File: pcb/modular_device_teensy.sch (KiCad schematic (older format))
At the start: 17 parts, among them P1 PWR_JACK_2.5x5.5_SMD_RA, P2 HEADER_01X03_SMD_RA, P3 HEADER_01X03_SMD_RA, P4 HEADER_01X03_SMD_RA, P5 BNC_DOUBLE_RA, P6 HEADER_01X02_SMD_RA, P7 HEADER_01X02_SMD_RA, SW1 KT_SWITCH

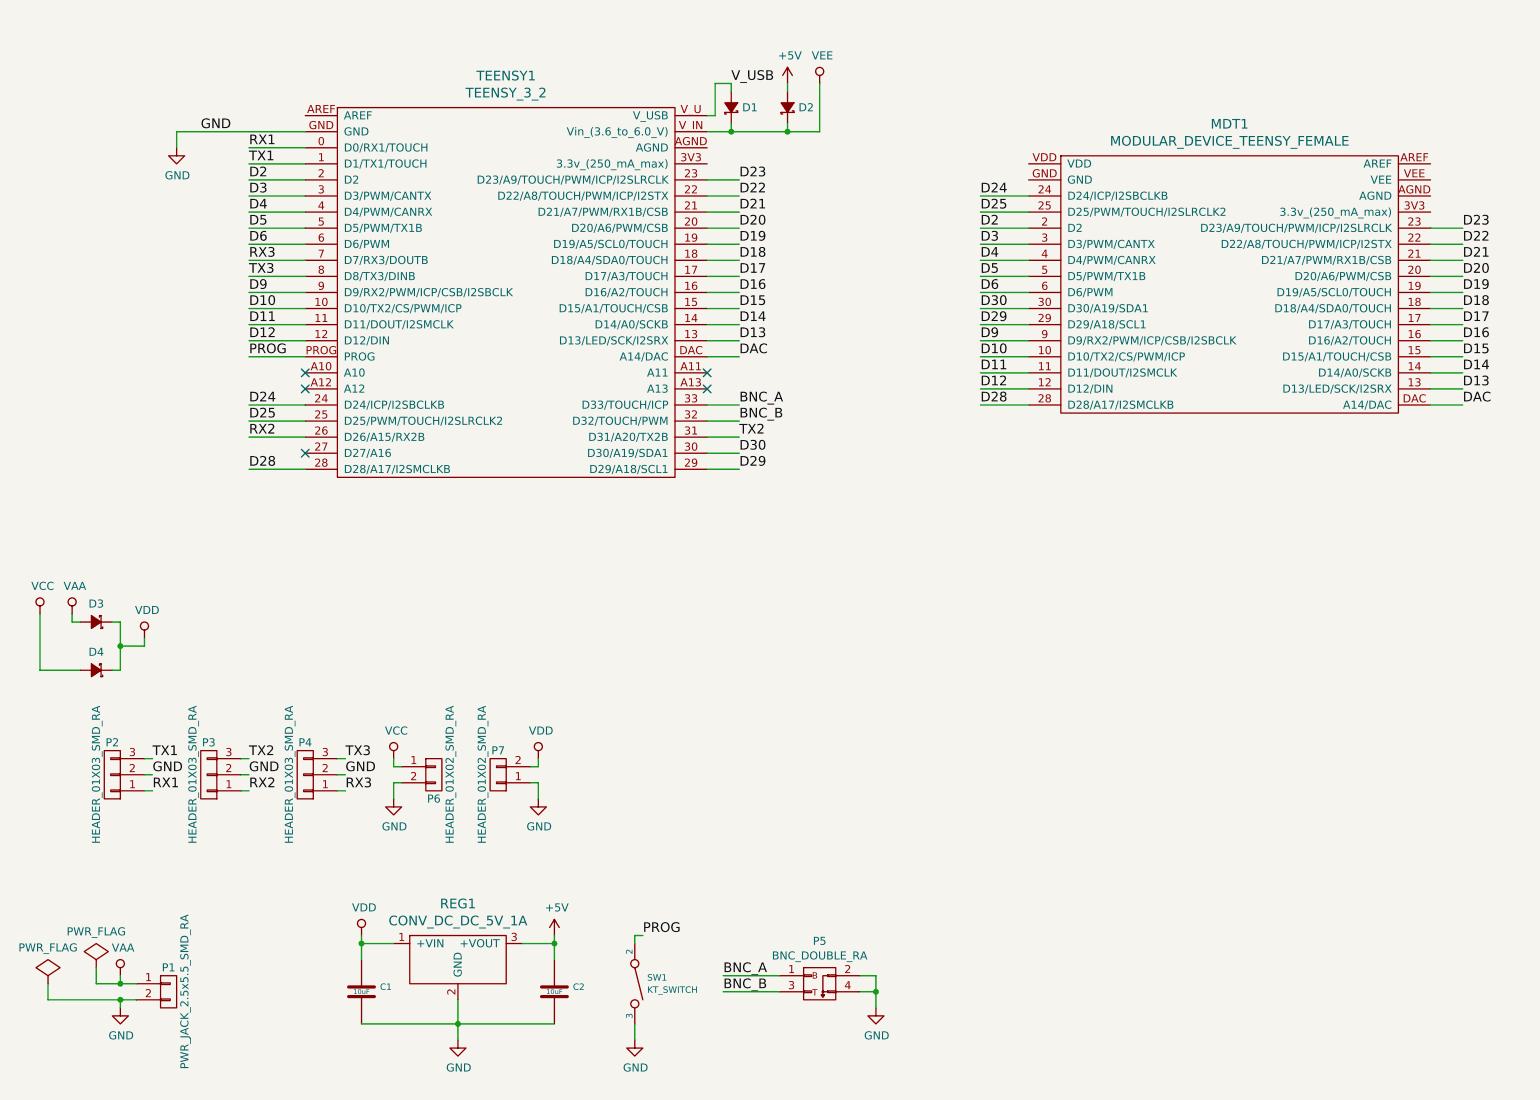
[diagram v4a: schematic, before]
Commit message: Progess towards new layout.
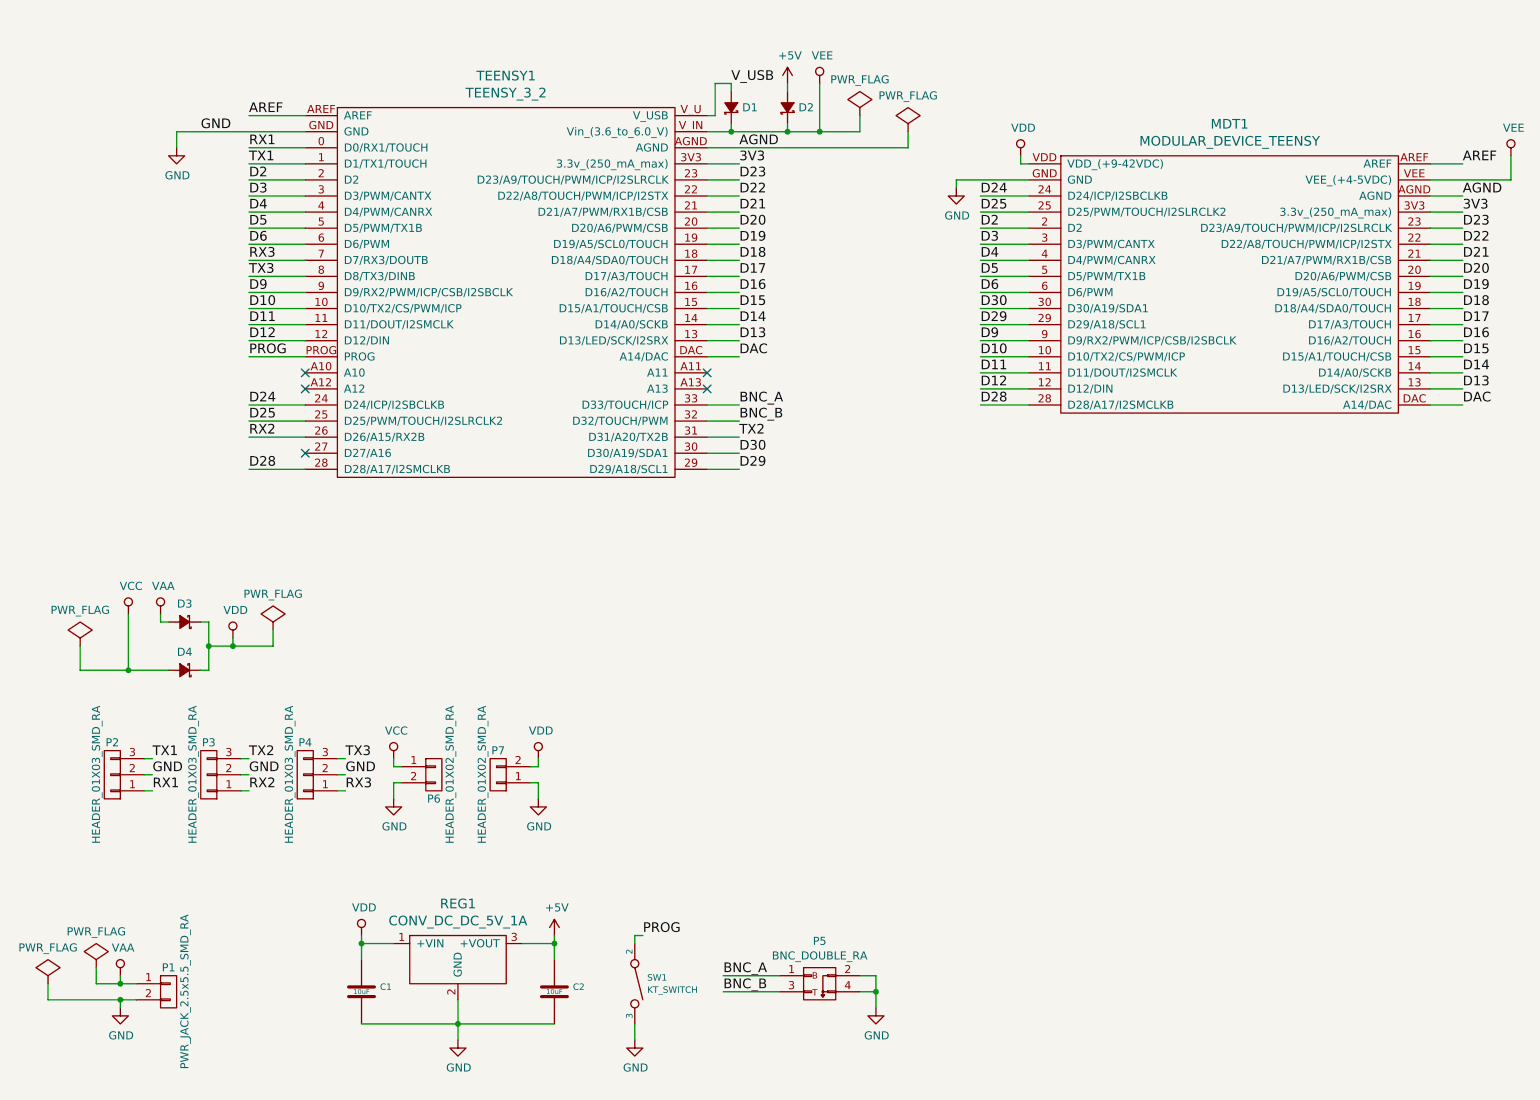
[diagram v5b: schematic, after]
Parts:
- removed MDT1: MODULAR_DEVICE_TEENSY_FEMALE, footprints:MODULAR_DEVICE_TEENSY_FEMALE, symbol MODULAR_DEVICE_TEENSY_FEMALE
- added MDT1: MODULAR_DEVICE_TEENSY, modular_device_teensy:MODULAR_DEVICE_TEENSY, symbol MODULAR_DEVICE_TEENSY
- SW1: footprint footprints:KT_SWITCH -> modular_device_teensy:KT_SWITCH
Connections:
- net D10: now also MDT1.10 (D10/TX2/CS/PWM/ICP)
- net D11: now also MDT1.11 (D11/DOUT/I2SMCLK)
- net D12: now also MDT1.12 (D12/DIN)
- net D13: now also MDT1.13 (D13/LED/SCK/I2SRX)
- net D14: now also MDT1.14 (D14/A0/SCKB)
- net D15: now also MDT1.15 (D15/A1/TOUCH/CSB)
- net D16: now also MDT1.16 (D16/A2/TOUCH)
- net D17: now also MDT1.17 (D17/A3/TOUCH)
- net D18: now also MDT1.18 (D18/A4/SDA0/TOUCH)
- net D19: now also MDT1.19 (D19/A5/SCL0/TOUCH)
- net D2: now also MDT1.2 (D2)
- net D20: now also MDT1.20 (D20/A6/PWM/CSB)
- net D21: now also MDT1.21 (D21/A7/PWM/RX1B/CSB)
- net D22: now also MDT1.22 (D22/A8/TOUCH/PWM/ICP/I2STX)
- net D23: now also MDT1.23 (D23/A9/TOUCH/PWM/ICP/I2SLRCLK)
- net D24: now also MDT1.24 (D24/ICP/I2SBCLKB)
- net D25: now also MDT1.25 (D25/PWM/TOUCH/I2SLRCLK2)
- net D28: now also MDT1.28 (D28/A17/I2SMCLKB)
- net D29: now also MDT1.29 (D29/A18/SCL1)
- net D3: now also MDT1.3 (D3/PWM/CANTX)
- net D30: now also MDT1.30 (D30/A19/SDA1)
- net D4: now also MDT1.4 (D4/PWM/CANRX)
- net D5: now also MDT1.5 (D5/PWM/TX1B)
- net D6: now also MDT1.6 (D6/PWM)
- net D9: now also MDT1.9 (D9/RX2/PWM/ICP/CSB/I2SBCLK)
- net DAC: now also MDT1.DAC (A14/DAC)
- net GND: now also MDT1.GND
- net VDD: now also MDT1.VDD (VDD_(+9-42VDC))
- net VEE: now also MDT1.VEE (VEE_(+4-5VDC))
- net 3V3: now reaches TEENSY1.3V3 (3.3v_(250_mA_max))
- net 3V3: now also MDT1.3V3 (3.3v_(250_mA_max))
- net AGND: now reaches TEENSY1.AGND
- net AGND: now also MDT1.AGND
- net AREF: now reaches TEENSY1.AREF
- net AREF: now also MDT1.AREF
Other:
- moved on the sheet: D3, D4
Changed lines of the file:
@@
 	4950 2050 4950 2100
 Wire Wire Line
-	4800 2100 5500 2100
+	4800 2100 5750 2100
 $Comp
 L +5V #PWR08
@@
 L VDD #PWR010
 U 1 1 576452DC
-P 1300 5250
-F 0 "#PWR010" H 1300 5100 50  0001 C CNN
-F 1 "VDD" H 1317 5423 50  0000 C CNN
-F 2 "" H 1300 5250 50  0000 C CNN
-F 3 "" H 1300 5250 50  0000 C CNN
-	1    1300 5250
+P 1850 5250
+F 0 "#PWR010" H 1850 5100 50  0001 C CNN
+F 1 "VDD" H 1867 5423 50  0000 C CNN
+F 2 "" H 1850 5250 50  0000 C CNN
+F 3 "" H 1850 5250 50  0000 C CNN
+	1    1850 5250
 	1    0    0    -1
 $EndComp
@@
 L diode_schottky_45V_10A D3
 U 1 1 5768305F
-P 1000 5150
-F 0 "D3" H 1000 5037 50  0000 C CNN
-F 1 "diode_schottky_45V_10A" H 720 5070 50  0001 L CNN
-F 2 "modular_device_teensy:CFP15" H 850 5130 60  0001 C CNN
-F 3 "" H 950 5230 60  0001 C CNN
-F 4 "digikey" H 1050 5330 60  0001 C CNN "Vendor"
-F 5 "568-11697-1-ND" H 1150 5430 60  0001 C CNN "PartNumber"
-F 6 "DIODE SCHOTTKY 45V 10A CFP15" H 1250 5530 60  0001 C CNN "Description"
-	1    1000 5150
+P 1550 5150
+F 0 "D3" H 1550 5037 50  0000 C CNN
+F 1 "diode_schottky_45V_10A" H 1270 5070 50  0001 L CNN
+F 2 "modular_device_teensy:CFP15" H 1400 5130 60  0001 C CNN
+F 3 "" H 1500 5230 60  0001 C CNN
+F 4 "digikey" H 1600 5330 60  0001 C CNN "Vendor"
+F 5 "568-11697-1-ND" H 1700 5430 60  0001 C CNN "PartNumber"
+F 6 "DIODE SCHOTTKY 45V 10A CFP15" H 1800 5530 60  0001 C CNN "Description"
+	1    1550 5150
 	-1   0    0    1
 $EndComp
@@
 L diode_schottky_45V_10A D4
 U 1 1 5768344A
-P 1000 5450
-F 0 "D4" H 1000 5337 50  0000 C CNN
-F 1 "diode_schottky_45V_10A" H 720 5370 50  0001 L CNN
-F 2 "modular_device_teensy:CFP15" H 850 5430 60  0001 C CNN
-F 3 "" H 950 5530 60  0001 C CNN
-F 4 "digikey" H 1050 5630 60  0001 C CNN "Vendor"
-F 5 "568-11697-1-ND" H 1150 5730 60  0001 C CNN "PartNumber"
-F 6 "DIODE SCHOTTKY 45V 10A CFP15" H 1250 5830 60  0001 C CNN "Description"
-	1    1000 5450
+P 1550 5450
+F 0 "D4" H 1550 5337 50  0000 C CNN
+F 1 "diode_schottky_45V_10A" H 1270 5370 50  0001 L CNN
+F 2 "modular_device_teensy:CFP15" H 1400 5430 60  0001 C CNN
+F 3 "" H 1500 5530 60  0001 C CNN
+F 4 "digikey" H 1600 5630 60  0001 C CNN "Vendor"
+F 5 "568-11697-1-ND" H 1700 5730 60  0001 C CNN "PartNumber"
+F 6 "DIODE SCHOTTKY 45V 10A CFP15" H 1800 5830 60  0001 C CNN "Description"
+	1    1550 5450
 	-1   0    0    1
 $EndComp
 Wire Wire Line
-	1100 5150 1150 5150
-Wire Wire Line
-	1150 5150 1150 5450
-Wire Wire Line
-	1150 5450 1100 5450
+	1650 5150 1700 5150
+Wire Wire Line
+	1700 5150 1700 5450
+Wire Wire Line
+	1700 5450 1650 5450
 $Comp
 L VAA #PWR013
 U 1 1 576834F6
-P 850 5100
-F 0 "#PWR013" H 850 4950 50  0001 C CNN
-F 1 "VAA" H 867 5273 50  0000 C CNN
-F 2 "" H 850 5100 50  0000 C CNN
-F 3 "" H 850 5100 50  0000 C CNN
-	1    850  5100
+P 1400 5100
+F 0 "#PWR013" H 1400 4950 50  0001 C CNN
+F 1 "VAA" H 1417 5273 50  0000 C CNN
+F 2 "" H 1400 5100 50  0000 C CNN
+F 3 "" H 1400 5100 50  0000 C CNN
+	1    1400 5100
 	1    0    0    -1
 $EndComp
@@
 L VCC #PWR014
 U 1 1 5768359B
-P 650 5100
-F 0 "#PWR014" H 650 4950 50  0001 C CNN
-F 1 "VCC" H 667 5273 50  0000 C CNN
-F 2 "" H 650 5100 50  0000 C CNN
-F 3 "" H 650 5100 50  0000 C CNN
-	1    650  5100
-	1    0    0    -1
-$EndComp
-Wire Wire Line
-	850  5100 850  5150
-Wire Wire Line
-	850  5150 900  5150
-Wire Wire Line
-	650  5100 650  5450
-Wire Wire Line
-	650  5450 900  5450
-Wire Wire Line
-	1150 5300 1300 5300
-Wire Wire Line
-	1300 5300 1300 5250
-Connection ~ 1150 5300
+P 1200 5100
+F 0 "#PWR014" H 1200 4950 50  0001 C CNN
+F 1 "VCC" H 1217 5273 50  0000 C CNN
+F 2 "" H 1200 5100 50  0000 C CNN
+F 3 "" H 1200 5100 50  0000 C CNN
+	1    1200 5100
+	1    0    0    -1
+$EndComp
+Wire Wire Line
+	1400 5100 1400 5150
+Wire Wire Line
+	1400 5150 1450 5150
+Wire Wire Line
+	1200 5100 1200 5450
+Wire Wire Line
+	900  5450 1450 5450
+Wire Wire Line
+	1700 5300 2100 5300
+Wire Wire Line
+	1850 5300 1850 5250
+Connection ~ 1700 5300
 $Comp
 L VDD #PWR015
@@
 F 0 "SW1" V 4312 7477 40  0000 L CNN
 F 1 "KT_SWITCH" V 4388 7477 40  0000 L CNN
-F 2 "footprints:KT_SWITCH" H 4250 7200 60  0001 C CNN
+F 2 "modular_device_teensy:KT_SWITCH" H 4250 7200 60  0001 C CNN
 F 3 "" H 4350 7350 60  0000 C CNN
 F 4 "digikey" H 4450 7600 60  0001 C CNN "Vendor"
@@
 Text Label 5000 3900 0    60   ~ 0
 BNC_B
-$Comp
-L MODULAR_DEVICE_TEENSY_FEMALE MDT1
-U 1 1 576DE218
-P 8050 3050
-F 0 "MDT1" H 8050 4047 60  0000 C CNN
-F 1 "MODULAR_DEVICE_TEENSY_FEMALE" H 8050 3941 60  0000 C CNN
-F 2 "footprints:MODULAR_DEVICE_TEENSY_FEMALE" H 8050 4100 60  0001 C CNN
-F 3 "" H 8100 5800 60  0000 C CNN
-F 4 "digikey" H 8050 4200 60  0001 C CNN "Vendor"
-F 5 "S7049-ND" H 8050 4300 60  0001 C CNN "PartNumber"
-F 6 "16 Position Header Through Hole" H 8050 4400 60  0001 C CNN "Description"
-	1    8050 3050
-	1    0    0    -1
-$EndComp
 Wire Wire Line
 	6800 2500 6500 2500
@@
 Text Label 9500 3800 0    60   ~ 0
 DAC
+$Comp
+L MODULAR_DEVICE_TEENSY MDT1
+U 1 1 57714506
+P 8050 3050
+F 0 "MDT1" H 8050 4047 60  0000 C CNN
+F 1 "MODULAR_DEVICE_TEENSY" H 8050 3941 60  0000 C CNN
+F 2 "modular_device_teensy:MODULAR_DEVICE_TEENSY" H 8050 4100 60  0001 C CNN
+F 3 "" H 8100 5800 60  0000 C CNN
+F 4 "digikey" H 8050 4200 60  0001 C CNN "Vendor"
+F 5 "S7049-ND" H 8050 4300 60  0001 C CNN "PartNumber"
+F 6 "16 Position Header Through Hole" H 8050 4400 60  0001 C CNN "Description"
+	1    8050 3050
+	1    0    0    -1
+$EndComp
+Wire Wire Line
+	2300 2000 1950 2000
+Text Label 1950 2000 0    60   ~ 0
+AREF
+Wire Wire Line
+	4800 2300 5000 2300
+Wire Wire Line
+	4800 2200 6050 2200
+Text Label 5000 2200 0    60   ~ 0
+AGND
+Text Label 5000 2300 0    60   ~ 0
+3V3
+Wire Wire Line
+	9300 2300 9500 2300
+Wire Wire Line
+	9300 2500 9500 2500
+Wire Wire Line
+	9300 2600 9500 2600
+Text Label 9500 2300 0    60   ~ 0
+AREF
+Text Label 9500 2500 0    60   ~ 0
+AGND
+Text Label 9500 2600 0    60   ~ 0
+3V3
+$Comp
+L GND #PWR020
+U 1 1 577150E0
+P 6350 2450
+F 0 "#PWR020" H 6350 2200 50  0001 C CNN
+F 1 "GND" H 6355 2277 50  0000 C CNN
+F 2 "" H 6350 2450 50  0000 C CNN
+F 3 "" H 6350 2450 50  0000 C CNN
+	1    6350 2450
+	1    0    0    -1
+$EndComp
+Wire Wire Line
+	6350 2450 6350 2400
+Wire Wire Line
+	6350 2400 6800 2400
+$Comp
+L VDD #PWR021
+U 1 1 577153D8
+P 6750 2250
+F 0 "#PWR021" H 6750 2100 50  0001 C CNN
+F 1 "VDD" H 6767 2423 50  0000 C CNN
+F 2 "" H 6750 2250 50  0000 C CNN
+F 3 "" H 6750 2250 50  0000 C CNN
+	1    6750 2250
+	1    0    0    -1
+$EndComp
+Wire Wire Line
+	6750 2250 6750 2300
+Wire Wire Line
+	6750 2300 6800 2300
+$Comp
+L VEE #PWR022
+U 1 1 57715626
+P 9800 2250
+F 0 "#PWR022" H 9800 2100 50  0001 C CNN
+F 1 "VEE" H 9817 2423 50  0000 C CNN
+F 2 "" H 9800 2250 50  0000 C CNN
+F 3 "" H 9800 2250 50  0000 C CNN
+	1    9800 2250
+	1    0    0    -1
+$EndComp
+Wire Wire Line
+	9300 2400 9800 2400
+Wire Wire Line
+	9800 2400 9800 2250
+$Comp
+L PWR_FLAG #FLG023
+U 1 1 577166D7
+P 5750 2000
+F 0 "#FLG023" H 5750 2095 50  0001 C CNN
+F 1 "PWR_FLAG" H 5750 2224 50  0000 C CNN
+F 2 "" H 5750 2000 50  0000 C CNN
+F 3 "" H 5750 2000 50  0000 C CNN
+	1    5750 2000
+	1    0    0    -1
+$EndComp
+Wire Wire Line
+	5750 2100 5750 2000
+Connection ~ 5500 2100
+$Comp
+L PWR_FLAG #FLG024
+U 1 1 57716880
+P 2100 5200
+F 0 "#FLG024" H 2100 5295 50  0001 C CNN
+F 1 "PWR_FLAG" H 2100 5424 50  0000 C CNN
+F 2 "" H 2100 5200 50  0000 C CNN
+F 3 "" H 2100 5200 50  0000 C CNN
+	1    2100 5200
+	1    0    0    -1
+$EndComp
+Wire Wire Line
+	2100 5300 2100 5200
+Connection ~ 1850 5300
+$Comp
+L PWR_FLAG #FLG025
+U 1 1 57716C30
+P 6050 2100
+F 0 "#FLG025" H 6050 2195 50  0001 C CNN
+F 1 "PWR_FLAG" H 6050 2324 50  0000 C CNN
+F 2 "" H 6050 2100 50  0000 C CNN
+F 3 "" H 6050 2100 50  0000 C CNN
+	1    6050 2100
+	1    0    0    -1
+$EndComp
+Wire Wire Line
+	6050 2200 6050 2100
+$Comp
+L PWR_FLAG #FLG026
+U 1 1 57716DFC
+P 900 5300
+F 0 "#FLG026" H 900 5395 50  0001 C CNN
+F 1 "PWR_FLAG" H 900 5524 50  0000 C CNN
+F 2 "" H 900 5300 50  0000 C CNN
+F 3 "" H 900 5300 50  0000 C CNN
+	1    900  5300
+	1    0    0    -1
+$EndComp
+Wire Wire Line
+	900  5300 900  5450
+Connection ~ 1200 5450
 $EndSCHEMATC
